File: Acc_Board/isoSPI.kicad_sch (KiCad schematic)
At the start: 14 parts, among them J2 IsoSPI

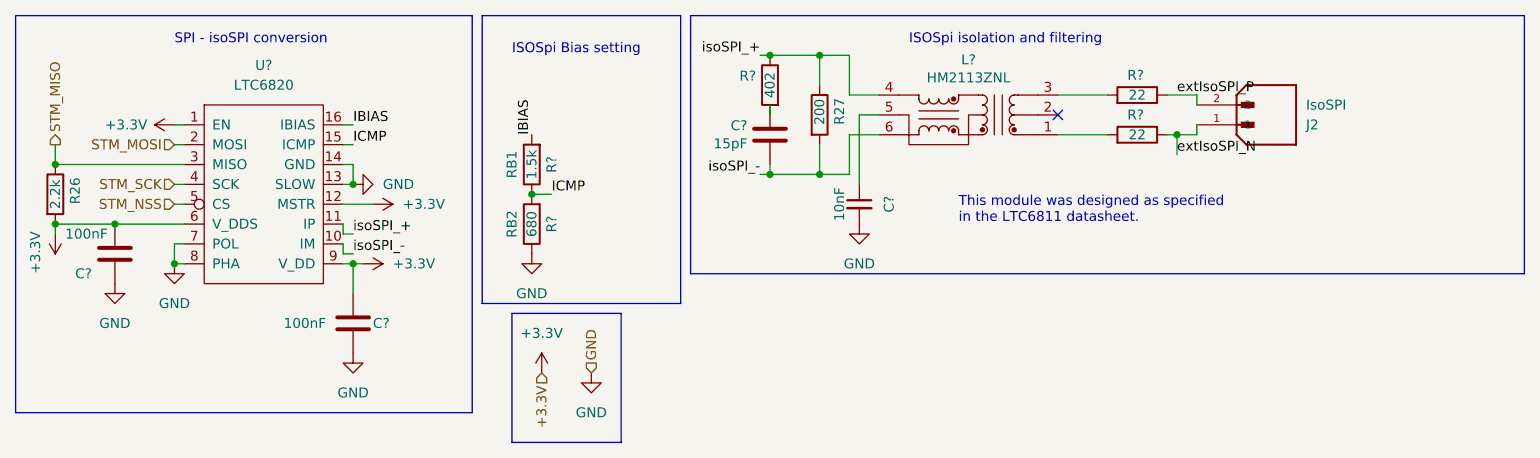
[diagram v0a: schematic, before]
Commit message: Acc board pcb updated to match schematic
more silkscreen work to do
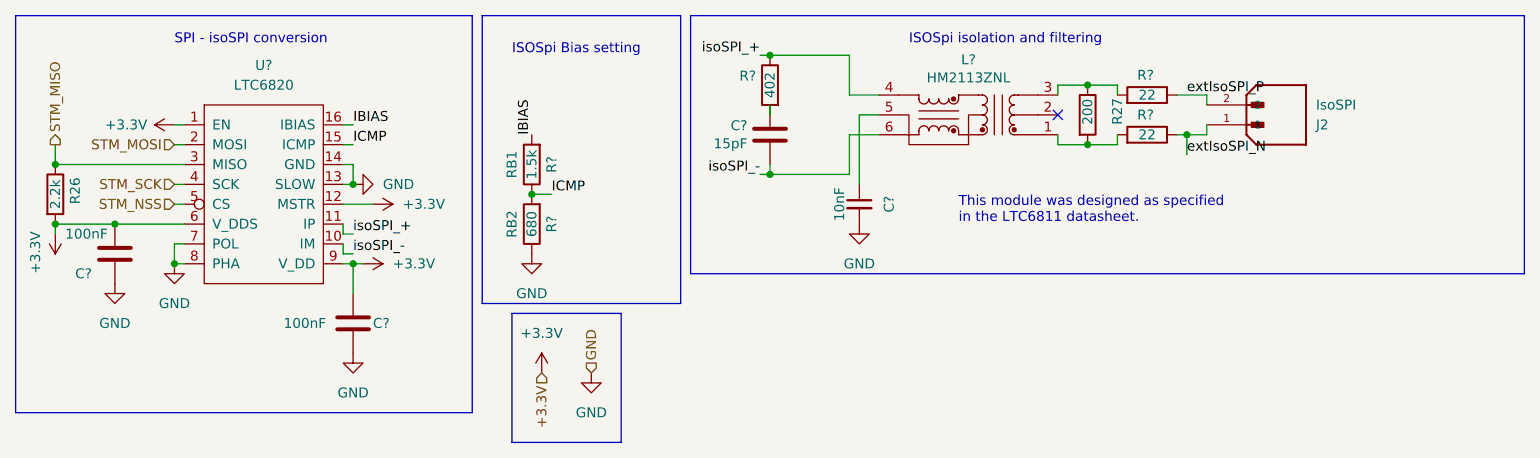
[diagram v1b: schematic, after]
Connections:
- net isoSPI_+: no longer R27.1
- net isoSPI_-: no longer R27.2
- net at L?.1, R?.2: now also R27.2
- net at L?.3, R?.2: now also R27.1
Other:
- moved on the sheet: J2, R27, R?
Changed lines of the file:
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@@
 	(paper "A4")
-	(junction
-		(at 118.11 41.91)
-		(diameter 0)
-		(color 0 0 0 0)
-	)
 	(junction
 		(at 20.32 48.26)
@@
 	)
 	(junction
-		(at 163.83 36.83)
-		(diameter 0)
-		(color 0 0 0 0)
-	)
-	(junction
-		(at 118.11 26.67)
+		(at 165.1 36.83)
 		(diameter 0)
 		(color 0 0 0 0)
@@
 	)
 	(junction
+		(at 152.4 30.48)
+		(diameter 0)
+		(color 0 0 0 0)
+	)
+	(junction
 		(at 35.56 53.34)
 		(diameter 0)
@@
 	)
 	(junction
+		(at 152.4 38.1)
+		(diameter 0)
+		(color 0 0 0 0)
+	)
+	(junction
 		(at 27.94 48.26)
 		(diameter 0)
@@
 	(wire
 		(pts
-			(xy 166.37 31.75) (xy 166.37 33.02)
-		)
-		(stroke
-			(width 0)
-			(type default)
-		)
-	)
-	(wire
-		(pts
-			(xy 111.76 26.67) (xy 118.11 26.67)
-		)
-		(stroke
-			(width 0)
-			(type default)
-		)
-	)
-	(wire
-		(pts
-			(xy 118.11 26.67) (xy 118.11 30.48)
+			(xy 167.64 31.75) (xy 167.64 33.02)
+		)
+		(stroke
+			(width 0)
+			(type default)
+		)
+	)
+	(wire
+		(pts
+			(xy 111.76 26.67) (xy 121.92 26.67)
+		)
+		(stroke
+			(width 0)
+			(type default)
+		)
+	)
+	(wire
+		(pts
+			(xy 156.21 30.48) (xy 156.21 31.75)
 		)
 		(stroke
@@
 	(wire
 		(pts
-			(xy 118.11 38.1) (xy 118.11 41.91)
+			(xy 148.59 30.48) (xy 148.59 31.75)
 		)
 		(stroke
@@
 	(wire
 		(pts
+			(xy 156.21 38.1) (xy 152.4 38.1)
+		)
+		(stroke
+			(width 0)
+			(type default)
+		)
+	)
+	(wire
+		(pts
 			(xy 58.42 35.56) (xy 57.15 35.56)
 		)
@@
 	(wire
 		(pts
-			(xy 148.59 31.75) (xy 154.94 31.75)
-		)
-		(stroke
-			(width 0)
-			(type default)
-		)
-	)
-	(wire
-		(pts
 			(xy 123.19 34.29) (xy 125.73 34.29)
 		)
@@
 	(wire
 		(pts
-			(xy 162.56 31.75) (xy 166.37 31.75)
-		)
-		(stroke
-			(width 0)
-			(type default)
-		)
-	)
-	(wire
-		(pts
-			(xy 118.11 41.91) (xy 121.92 41.91)
+			(xy 163.83 31.75) (xy 167.64 31.75)
 		)
 		(stroke
@@
 	(wire
 		(pts
-			(xy 163.83 39.37) (xy 163.83 36.83)
-		)
-		(stroke
-			(width 0)
-			(type default)
-		)
-	)
-	(wire
-		(pts
-			(xy 166.37 35.56) (xy 166.37 36.83)
+			(xy 148.59 38.1) (xy 148.59 36.83)
+		)
+		(stroke
+			(width 0)
+			(type default)
+		)
+	)
+	(wire
+		(pts
+			(xy 165.1 39.37) (xy 165.1 36.83)
+		)
+		(stroke
+			(width 0)
+			(type default)
+		)
+	)
+	(wire
+		(pts
+			(xy 167.64 35.56) (xy 167.64 36.83)
+		)
+		(stroke
+			(width 0)
+			(type default)
+		)
+	)
+	(wire
+		(pts
+			(xy 152.4 30.48) (xy 156.21 30.48)
 		)
 		(stroke
@@
 	(wire
 		(pts
-			(xy 166.37 36.83) (xy 163.83 36.83)
+			(xy 167.64 36.83) (xy 165.1 36.83)
 		)
 		(stroke
@@
 	(wire
 		(pts
-			(xy 148.59 36.83) (xy 154.94 36.83)
-		)
-		(stroke
-			(width 0)
-			(type default)
-		)
-	)
-	(wire
-		(pts
-			(xy 118.11 26.67) (xy 121.92 26.67)
-		)
-		(stroke
-			(width 0)
-			(type default)
-		)
-	)
-	(wire
-		(pts
-			(xy 111.76 41.91) (xy 118.11 41.91)
+			(xy 148.59 38.1) (xy 152.4 38.1)
+		)
+		(stroke
+			(width 0)
+			(type default)
+		)
+	)
+	(wire
+		(pts
+			(xy 111.76 41.91) (xy 121.92 41.91)
 		)
 		(stroke
@@
 		)
 	)
+	(wire
+		(pts
+			(xy 152.4 30.48) (xy 148.59 30.48)
+		)
+		(stroke
+			(width 0)
+			(type default)
+		)
+	)
 	(polyline
 		(pts
@@
 	(wire
 		(pts
-			(xy 163.83 36.83) (xy 162.56 36.83)
+			(xy 165.1 36.83) (xy 163.83 36.83)
+		)
+		(stroke
+			(width 0)
+			(type default)
+		)
+	)
+	(wire
+		(pts
+			(xy 156.21 38.1) (xy 156.21 36.83)
 		)
 		(stroke
@@
 	)
 	(label "extIsoSPI_N"
-		(at 163.83 39.37 0)
+		(at 165.1 39.37 0)
 		(fields_autoplaced yes)
 		(effects
@@
 	)
 	(label "extIsoSPI_P"
-		(at 163.83 31.75 0)
+		(at 165.1 31.75 0)
 		(fields_autoplaced yes)
 		(effects
@@
 	(symbol
 		(lib_id "Device:R")
-		(at 118.11 34.29 0)
+		(at 152.4 34.29 0)
 		(unit 1)
 		(exclude_from_sim no)
@@
 		(dnp no)
 		(property "Reference" "R27"
-			(at 120.65 35.56 90)
+			(at 156.21 35.56 90)
 			(effects
 				(font
@@
 		)
 		(property "Value" "200"
-			(at 118.11 35.56 90)
+			(at 152.4 35.56 90)
 			(effects
 				(font
@@
 		)
 		(property "Footprint" "Resistor_SMD:R_0805_2012Metric_Pad1.20x1.40mm_HandSolder"
-			(at 116.332 34.29 90)
+			(at 150.622 34.29 90)
 			(effects
 				(font
@@
 		)
 		(property "Datasheet" "~"
-			(at 118.11 34.29 0)
+			(at 152.4 34.29 0)
 			(effects
 				(font
@@
 		)
 		(property "Description" ""
-			(at 118.11 34.29 0)
+			(at 152.4 34.29 0)
 			(effects
 				(font
@@
 	(symbol
 		(lib_id "Device:R")
-		(at 158.75 36.83 270)
+		(at 160.02 36.83 270)
 		(mirror x)
 		(unit 1)
@@
 		(dnp no)
 		(property "Reference" "R?"
-			(at 157.48 34.29 90)
+			(at 158.75 34.29 90)
 			(effects
 				(font
@@
 		)
 		(property "Value" "22"
-			(at 158.75 36.83 90)
+			(at 160.02 36.83 90)
 			(effects
 				(font
@@
 		)
 		(property "Footprint" "Resistor_SMD:R_0805_2012Metric_Pad1.20x1.40mm_HandSolder"
-			(at 158.75 38.608 90)
+			(at 160.02 38.608 90)
 			(effects
 				(font
@@
 		)
 		(property "Datasheet" "~"
-			(at 158.75 36.83 0)
+			(at 160.02 36.83 0)
 			(effects
 				(font
@@
 		)
 		(property "Description" ""
-			(at 158.75 36.83 0)
+			(at 160.02 36.83 0)
 			(effects
 				(font
@@
 	(symbol
 		(lib_id "1FS_2_Global_Symbol_Library:1053091202")
-		(at 171.45 35.56 0)
+		(at 172.72 35.56 0)
 		(mirror x)
 		(unit 1)
@@
 		(dnp no)
 		(property "Reference" "J2"
-			(at 180.34 35.56 0)
+			(at 181.61 35.56 0)
 			(effects
 				(font
@@
 		)
 		(property "Value" "IsoSPI"
-			(at 180.34 33.02 0)
+			(at 181.61 33.02 0)
 			(effects
 				(font
@@
 		)
 		(property "Footprint" "1FS_2_Global_Footprint_Library:MOLEX_1053091202"
-			(at 171.45 35.56 0)
+			(at 172.72 35.56 0)
 			(effects
 				(font
@@
 		)
 		(property "Datasheet" ""
-			(at 171.45 35.56 0)
+			(at 172.72 35.56 0)
 			(effects
 				(font
@@
 		)
 		(property "Description" ""
-			(at 171.45 35.56 0)
+			(at 172.72 35.56 0)
 			(effects
 				(font
@@
 		)
 		(property "PARTREV" "H"
-			(at 171.45 35.56 0)
+			(at 172.72 35.56 0)
 			(effects
 				(font
@@
 		)
 		(property "STANDARD" "Manufacturer Recommendations"
-			(at 171.45 35.56 0)
+			(at 172.72 35.56 0)
 			(effects
 				(font
@@
 		)
 		(property "MAXIMUM_PACKAGE_HEIGHT" "10.51 mm"
-			(at 171.45 35.56 0)
+			(at 172.72 35.56 0)
 			(effects
 				(font
@@
 		)
 		(property "MANUFACTURER" "Molex"
-			(at 171.45 35.56 0)
+			(at 172.72 35.56 0)
 			(effects
 				(font
@@
 	(symbol
 		(lib_id "Device:R")
-		(at 158.75 31.75 270)
+		(at 160.02 31.75 270)
 		(mirror x)
 		(unit 1)
@@
 		(dnp no)
 		(property "Reference" "R?"
-			(at 157.48 29.21 90)
+			(at 158.75 29.21 90)
 			(effects
 				(font
@@
 		)
 		(property "Value" "22"
-			(at 158.75 31.75 90)
+			(at 160.02 31.75 90)
 			(effects
 				(font
@@
 		)
 		(property "Footprint" "Resistor_SMD:R_0805_2012Metric_Pad1.20x1.40mm_HandSolder"
-			(at 158.75 33.528 90)
+			(at 160.02 33.528 90)
 			(effects
 				(font
@@
 		)
 		(property "Datasheet" "~"
-			(at 158.75 31.75 0)
+			(at 160.02 31.75 0)
 			(effects
 				(font
@@
 		)
 		(property "Description" ""
-			(at 158.75 31.75 0)
-			(effects
-				(font
+			(at 160.02 31.75 0)
+			(effects
+				(font

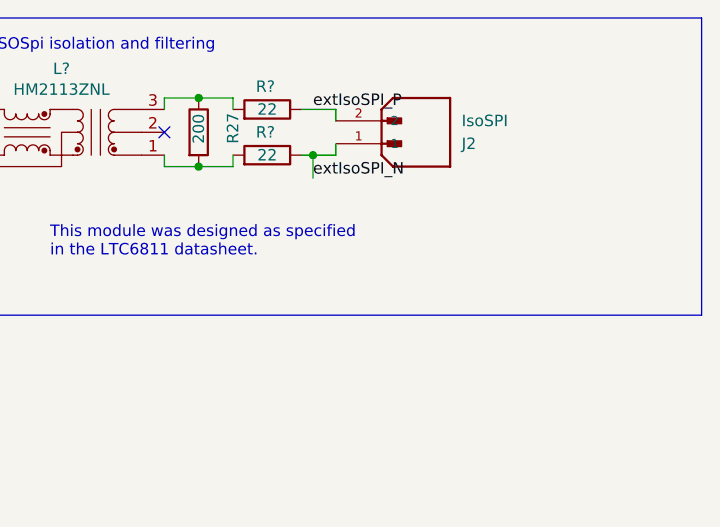
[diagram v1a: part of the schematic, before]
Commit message: Acc Board test points added
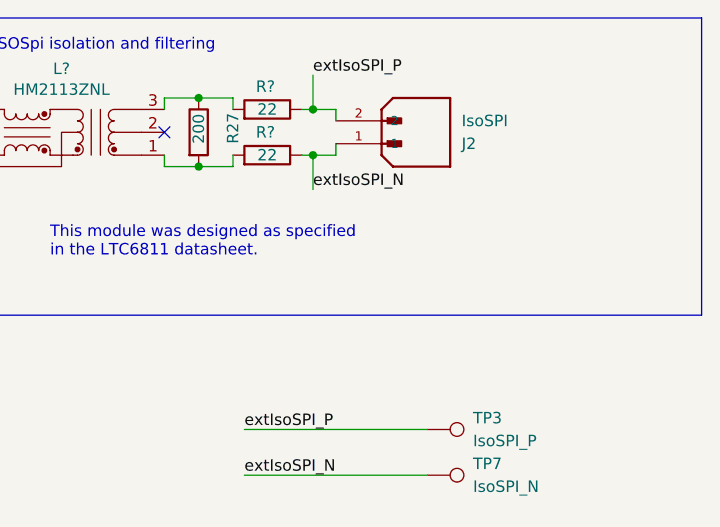
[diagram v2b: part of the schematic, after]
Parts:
- added TP3: IsoSPI_P, TestPoint:TestPoint_Loop_D2.50mm_Drill1.0mm, symbol Connector:TestPoint
- added TP7: IsoSPI_N, TestPoint:TestPoint_Loop_D2.50mm_Drill1.0mm, symbol Connector:TestPoint
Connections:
- net extIsoSPI_N: now also TP7.1
- net extIsoSPI_P: now also TP3.1
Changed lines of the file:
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@@
+		(color 0 0 0 0)
+	)
+	(junction
+		(at 165.1 31.75)
+		(diameter 0)
 		(color 0 0 0 0)
 	)
@@
 	(wire
 		(pts
+			(xy 157.48 67.31) (xy 177.8 67.31)
+		)
+		(stroke
+			(width 0)
+			(type default)
+		)
+	)
+	(wire
+		(pts
 			(xy 35.56 50.8) (xy 36.83 50.8)
 		)
@@
 	(wire
 		(pts
+			(xy 165.1 27.94) (xy 165.1 31.75)
+		)
+		(stroke
+			(width 0)
+			(type default)
+		)
+	)
+	(wire
+		(pts
 			(xy 167.64 31.75) (xy 167.64 33.02)
 		)
@@
 	(wire
 		(pts
+			(xy 157.48 72.39) (xy 177.8 72.39)
+		)
+		(stroke
+			(width 0)
+			(type default)
+		)
+	)
+	(wire
+		(pts
 			(xy 35.56 45.72) (xy 36.83 45.72)
 		)
@@
 	(wire
 		(pts
-			(xy 163.83 31.75) (xy 167.64 31.75)
+			(xy 163.83 31.75) (xy 165.1 31.75)
 		)
 		(stroke
@@
 	(wire
 		(pts
-			(xy 165.1 39.37) (xy 165.1 36.83)
+			(xy 165.1 40.64) (xy 165.1 36.83)
 		)
 		(stroke
@@
 		(pts
 			(xy 156.21 38.1) (xy 156.21 36.83)
+		)
+		(stroke
+			(width 0)
+			(type default)
+		)
+	)
+	(wire
+		(pts
+			(xy 165.1 31.75) (xy 167.64 31.75)
 		)
 		(stroke
@@
 	)
 	(label "extIsoSPI_N"
-		(at 165.1 39.37 0)
+		(at 165.1 40.64 0)
 		(fields_autoplaced yes)
 		(effects
@@
 		)
 	)
-	(label "IBIAS"
-		(at 81.28 36.83 90)
+	(label "extIsoSPI_P"
+		(at 157.48 67.31 0)
 		(fields_autoplaced yes)
 		(effects
@@
 		)
 	)
+	(label "IBIAS"
+		(at 81.28 36.83 90)
+		(fields_autoplaced yes)
+		(effects
+			(font
+				(size 1.27 1.27)
+			)
+			(justify left bottom)
+		)
+	)
+	(label "extIsoSPI_N"
+		(at 157.48 72.39 0)
+		(fields_autoplaced yes)
+		(effects
+			(font
+				(size 1.27 1.27)
+			)
+			(justify left bottom)
+		)
+	)
 	(label "extIsoSPI_P"
-		(at 165.1 31.75 0)
+		(at 165.1 27.94 0)
 		(fields_autoplaced yes)
 		(effects
@@
 	)
 	(symbol
+		(lib_id "Connector:TestPoint")
+		(at 177.8 67.31 270)
+		(unit 1)
+		(exclude_from_sim no)
+		(in_bom yes)
+		(on_board yes)
+		(dnp no)
+		(fields_autoplaced yes)
+		(property "Reference" "TP3"
+			(at 182.88 66.0399 90)
+			(effects
+				(font
+					(size 1.27 1.27)
+				)
+				(justify left)
+			)
+		)
+		(property "Value" "IsoSPI_P"
+			(at 182.88 68.5799 90)
+			(effects
+				(font
+					(size 1.27 1.27)
+				)
+				(justify left)
+			)
+		)
+		(property "Footprint" "TestPoint:TestPoint_Loop_D2.50mm_Drill1.0mm"
+			(at 177.8 72.39 0)
+			(effects
+				(font
+					(size 1.27 1.27)
+				)
+				(hide yes)
+			)
+		)
+		(property "Datasheet" "~"
+			(at 177.8 72.39 0)
+			(effects
+				(font
+					(size 1.27 1.27)
+				)
+				(hide yes)
+			)
+		)
+		(property "Description" "test point"
+			(at 177.8 67.31 0)
+			(effects
+				(font
+					(size 1.27 1.27)
+				)
+				(hide yes)
+			)
+		)
+		(pin "1"
+		)
+		(instances
+			(project "Acc_Board"
+				(path "/e19d26dd-723b-45e6-9d59-b1730158e759/418586a7-bc6a-480e-8435-4a2eb96d1e0c"
+					(reference "TP3")
+					(unit 1)
+				)
+			)
+		)
+	)
+	(symbol
 		(lib_id "power:+3.3V")
 		(at 20.32 49.53 180)
@@
 					(unit 1)
 				)
+			)
+		)
+	)
+	(symbol
+		(lib_id "Connector:TestPoint")
+		(at 177.8 72.39 270)
+		(unit 1)
+		(exclude_from_sim no)
+		(in_bom yes)
+		(on_board yes)
+		(dnp no)
+		(fields_autoplaced yes)
+		(property "Reference" "TP7"
+			(at 182.88 71.1199 90)
+			(effects
+				(font
+					(size 1.27 1.27)
+				)
+				(justify left)
+			)
+		)
+		(property "Value" "IsoSPI_N"
+			(at 182.88 73.6599 90)
+			(effects
+				(font
+					(size 1.27 1.27)
+				)
+				(justify left)
+			)
+		)
+		(property "Footprint" "TestPoint:TestPoint_Loop_D2.50mm_Drill1.0mm"
+			(at 177.8 77.47 0)
+			(effects
+				(font
+					(size 1.27 1.27)
+				)
+				(hide yes)
+			)
+		)
+		(property "Datasheet" "~"
+			(at 177.8 77.47 0)
+			(effects
+				(font
+					(size 1.27 1.27)
+				)
+				(hide yes)
+			)
+		)
+		(property "Description" "test point"
+			(at 177.8 72.39 0)
+			(effects
+				(font
+					(size 1.27 1.27)
+				)
+				(hide yes)
+			)
+		)
+		(pin "1"
+		)
+		(instances
+			(project "Acc_Board"
+				(path "/e19d26dd-723b-45e6-9d59-b1730158e759/418586a7-bc6a-480e-8435-4a2eb96d1e0c"
+					(reference "TP7")
+					(unit 1)
+				)
